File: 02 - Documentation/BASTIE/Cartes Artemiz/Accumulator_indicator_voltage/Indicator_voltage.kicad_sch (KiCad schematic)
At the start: 19 parts, among them J7 2P Droit 2-11-2022, Q1 NMOS SQ2348ES-T1_GE3

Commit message: Revert "Delete kicad_prl"
This reverts commit 9fe5be2906406c3c64afc6048a7ffd3d023d0e3c.
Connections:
- net 0: no longer PS1.4 (TRIM), PS1.6 (REMOTE_ON/OFF)
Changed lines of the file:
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@@
-	)
-	(junction
-		(at 88.9 43.18)
-		(diameter 0)
-		(color 0 0 0 0)
-	)
-	(junction
-		(at 142.24 43.18)
-		(diameter 0)
-		(color 0 0 0 0)
 	)
 	(junction
@@
 	(wire
 		(pts
-			(xy 88.9 43.18) (xy 88.9 48.26)
-		)
-		(stroke
-			(width 0)
-			(type default)
-		)
-	)
-	(wire
-		(pts
-			(xy 142.24 43.18) (xy 142.24 60.96)
+			(xy 142.24 40.64) (xy 142.24 60.96)
 		)
 		(stroke
@@
 	(wire
 		(pts
-			(xy 142.24 40.64) (xy 142.24 43.18)
-		)
-		(stroke
-			(width 0)
-			(type default)
-		)
-	)
-	(wire
-		(pts
 			(xy 142.24 38.1) (xy 142.24 33.02)
 		)
@@
 	(wire
 		(pts
-			(xy 138.43 43.18) (xy 142.24 43.18)
-		)
-		(stroke
-			(width 0)
-			(type default)
-		)
-	)
-	(wire
-		(pts
 			(xy 119.38 134.62) (xy 130.81 134.62)
 		)
@@
 	(wire
 		(pts
-			(xy 88.9 43.18) (xy 92.71 43.18)
-		)
-		(stroke
-			(width 0)
-			(type default)
-		)
-	)
-	(wire
-		(pts
 			(xy 59.69 146.05) (xy 64.77 146.05)
 		)
@@
 	(wire
 		(pts
-			(xy 88.9 40.64) (xy 88.9 43.18)
-		)
-		(stroke
+			(xy 88.9 40.64) (xy 88.9 48.26)
+		)
+		(stroke

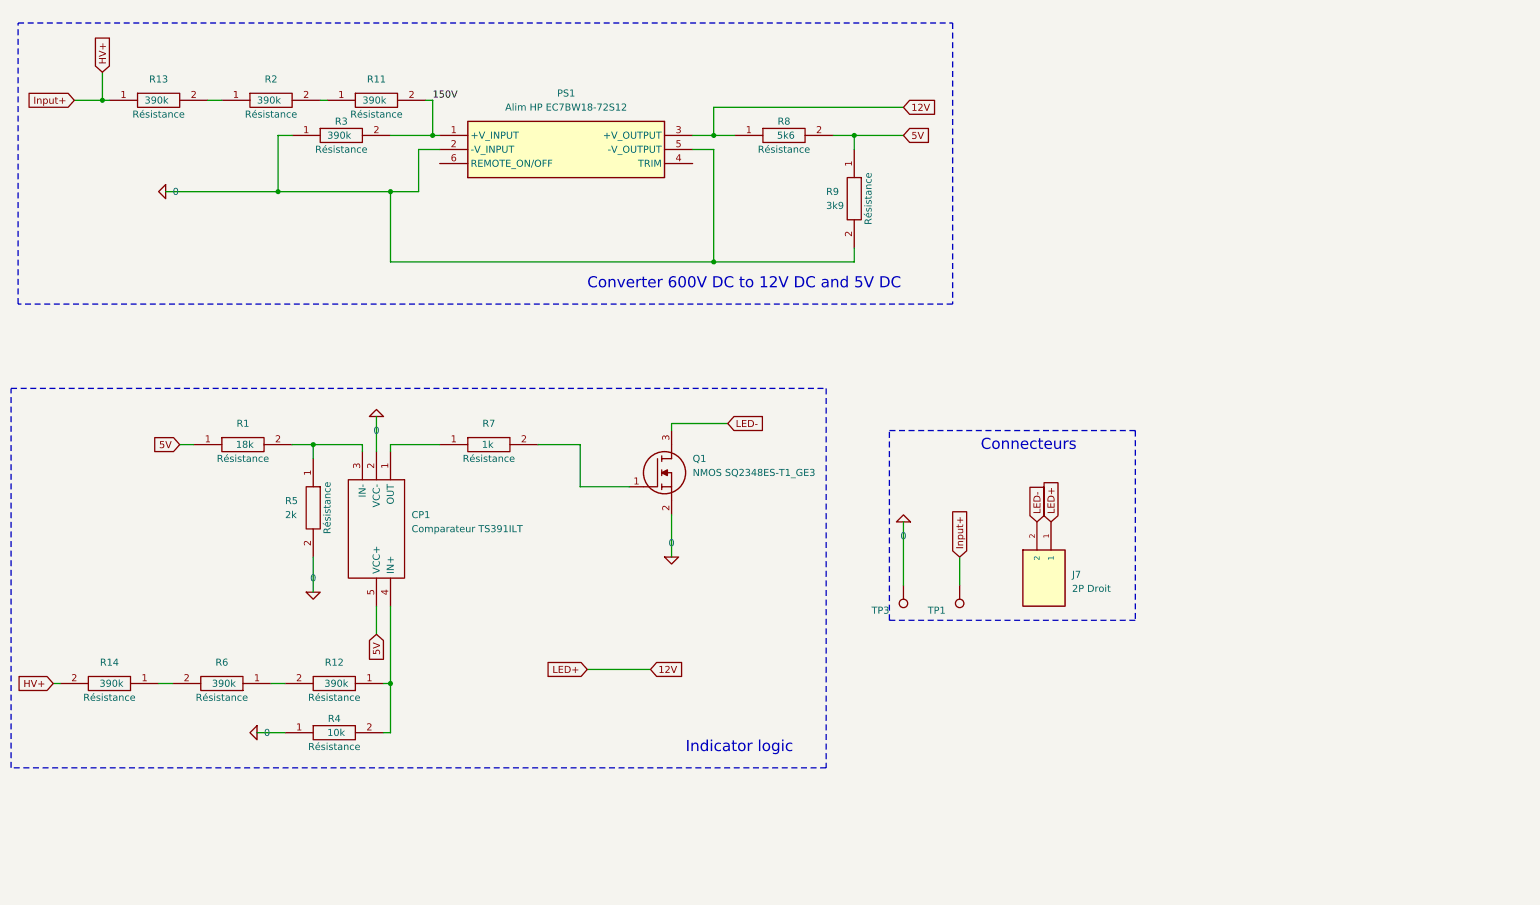
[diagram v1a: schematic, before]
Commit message: Working Voltage indicator
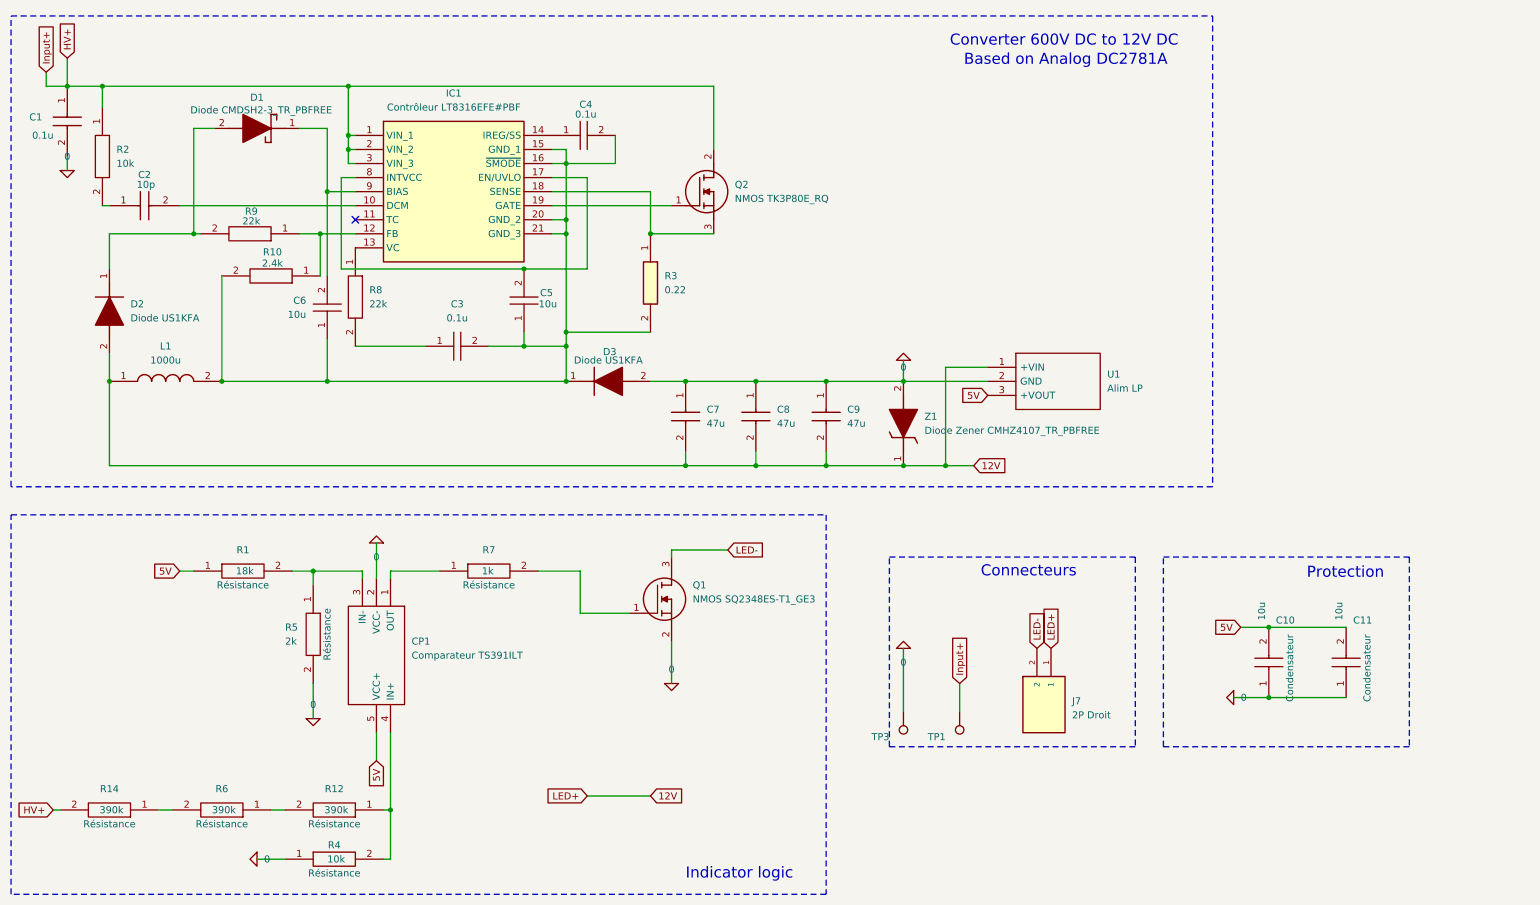
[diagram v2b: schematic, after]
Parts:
- removed PS1: Alim HP EC7BW18-72S12, EC7BW1872S12, symbol EPSAlib:Alim HP EC7BW18-72S12
- removed R11, R13, R2, R3: 390k, EPSA_lib:RESC3216X70N, symbol EPSA_lib:Résistance RK73H2BLTDD2152F
- removed R8: 5k6, EPSA_lib:RESC3216X70N, symbol EPSA_lib:Résistance RK73H2BLTDD2152F
- removed R9: 3k9, EPSA_lib:RESC3216X70N, symbol EPSA_lib:Résistance RK73H2BLTDD2152F
- added C1: 0.1u, CAPC4532X200N, symbol EPSAlib:Condensateur HV GCJ43DR72J104KXJ1L
- added C10, C11: 10u, EPSA:CAPC2012X130N, symbol EPSA_lib:Condensateur 0805Y1000104JXT
- added C2: 10p, CAPC3216X100N, symbol EPSAlib:Condensateur HV GRM31A5C2J100JW01D
- added C3, C4: 0.1u, EPSA_lib:CAPC2012X130N, symbol EPSAlib:Condensateur 0805Y1000104JXT
- added C5, C6: 10u, EPSA_lib:CAPC2012X130N, symbol EPSAlib:Condensateur 0805Y1000104JXT
- added C7, C8, C9: 47u, CAPC3225X270N, symbol EPSAlib:Condensateur GRM32ER61C476KE15K
- added D1: Diode CMDSH2-3_TR_PBFREE, SOD2512X110N, symbol EPSAlib:Diode CMDSH2-3_TR_PBFREE
- added D2, D3: Diode US1KFA, SODFL3618X143N, symbol EPSAlib:Diode US1KFA
- added IC1: Contrôleur LT8316EFE#PBF, LT8315EFEPBF, symbol EPSAlib:Contrôleur LT8316EFE#PBF
- added L1: 1000u, WE-PD_1260/1245/1280/121054, symbol EPSAlib:Bobine 7447709102
- added Q2: NMOS TK3P80E_RQ, TK3P80ERQ, symbol EPSAlib:NMOS TK3P80E_RQ
- added R10: 2.4k, EPSA_lib:RESC3216X70N, symbol EPSAlib:Résistance RK73H2BLTDD2152F
- added R2: 10k, EPSA_lib:RESC3216X70N, symbol EPSAlib:Résistance RK73H2BLTDD2152F
- added R3: 0.22, RESC1608X55N, symbol EPSAlib:Résistance RL0816S-R22-F
- added R8, R9: 22k, EPSA_lib:RESC3216X70N, symbol EPSAlib:Résistance RK73H2BLTDD2152F
- added U1: Alim LP TSR_0.5-2450, EPSA_lib:TSR-0.5-2433, symbol EPSAlib:Alim LP TSR_0.5-2450
- added Z1: Diode Zener CMHZ4107_TR_PBFREE, SOD3816X135N, symbol EPSAlib:Diode Zener CMHZ4107_TR_PBFREE
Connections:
- net 0: now also C1.2, C10.1, C11.1, C7.1, C8.1, C9.1, D3.2 (A), U1.2 (GND), Z1.2 (A)
- net 12V: now also C7.2, C8.2, C9.2, D2.2 (A), L1.1, U1.1 (+VIN), Z1.1 (K)
- net 5V: now also C10.2, C11.2, U1.3 (+VOUT)
- net HV+: now also C1.1, IC1.1 (VIN_1), IC1.2 (VIN_2), IC1.3 (VIN_3), Q2.2 (D), R2.1
- new net: C4.1, IC1.14 (IREG/SS)
- new net: C3.2, C4.2, C5.1, C6.1, D3.1 (K), IC1.15 (GND_1), IC1.16 (~{SMODE}), IC1.20 (GND_2), IC1.21 (GND_3), L1.2, R10.2, R3.2
- new net: C2.1, R2.2
- new net: C2.2, IC1.10 (DCM)
- new net: C6.2, D1.1 (K), IC1.9 (BIAS)
- new net: D1.2 (A), D2.1 (K), R9.2
- new net: IC1.13 (VC), R8.1
- new net: C3.1, R8.2
- new net: IC1.12 (FB), R10.1, R9.1
- new net: IC1.18 (SENSE), Q2.3 (S), R3.1
- new net: C5.2, IC1.17 (EN/UVLO), IC1.8 (INTVCC)
- new net: IC1.19 (GATE), Q2.1 (G)
- no-connect marks 0 -> 1
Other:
- note added: "Based on Analog DC2781A"
- note added: "Converter 600V DC to 12V DC"
- note added: "Protection"
- note removed: "Converter 600V DC to 12V DC and 5V DC"
- moved on the sheet: CP1, J7, Q1, R1, R12, R14, R4, R5, R6, R7, TP1, TP3

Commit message: TS et charger schematic pour école de ski français
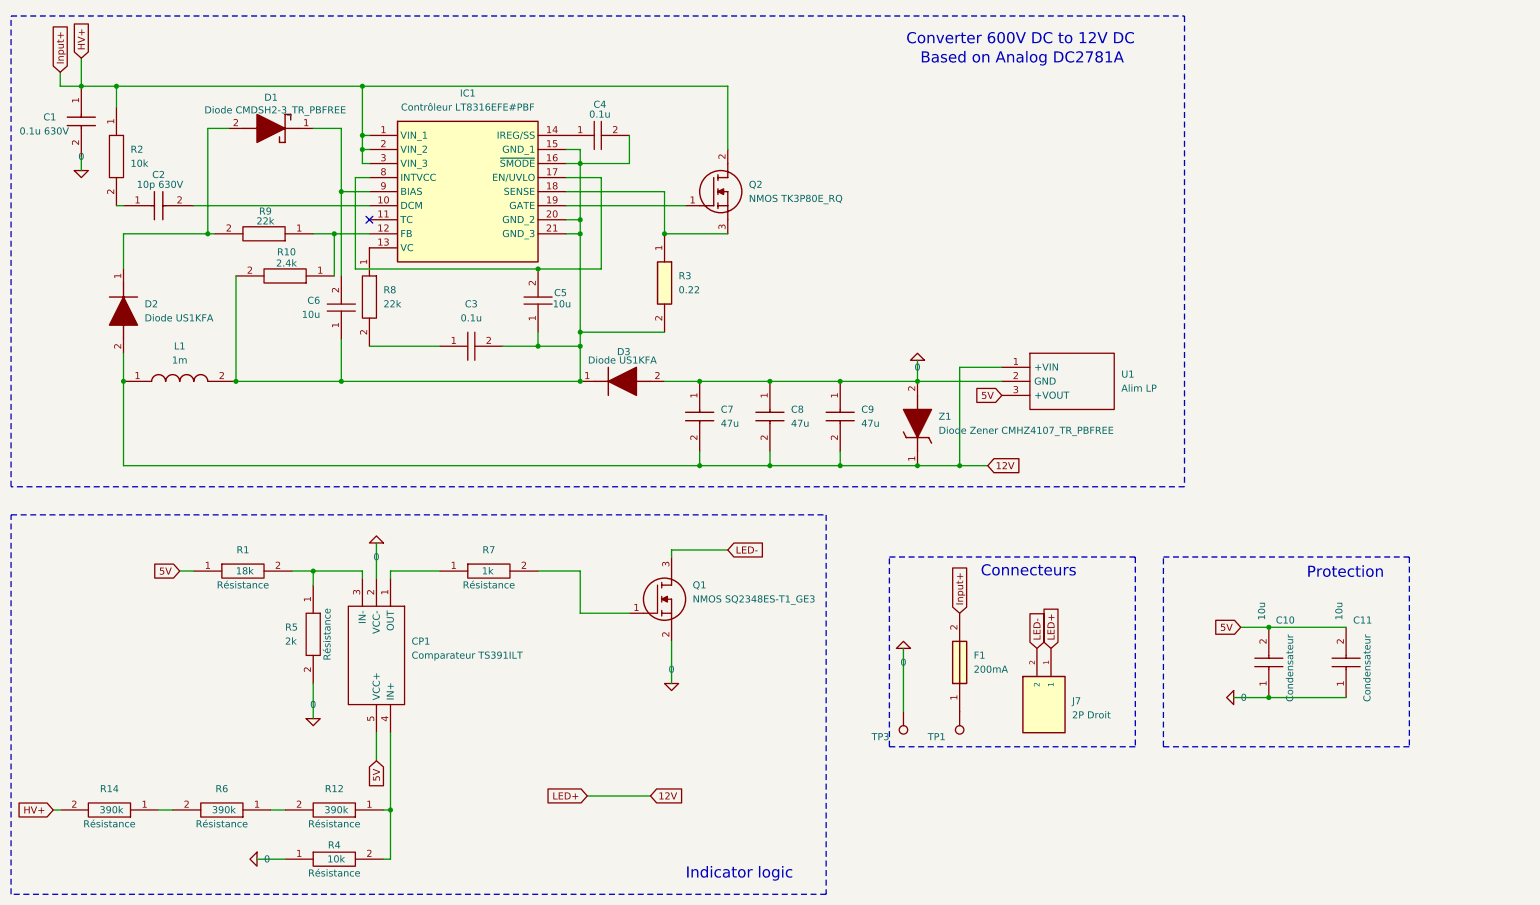
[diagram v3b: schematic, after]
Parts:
- added F1: 200mA, 0ADAP0200RE, symbol EPSAlib:Fusible 0ADAP0200-RE
- C1: value 0.1u -> 0.1u 630V
- C2: value 10p -> 10p 630V
- L1: value 1000u -> 1m
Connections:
- net HV+: now also F1.2; no longer TP1.1
- new net: F1.1, TP1.1
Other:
- moved on the sheet: C1, C2, C3, C4, C5, C6, C7, C8, C9, D1, D2, D3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

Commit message: Légères corrections Indicator Voltage
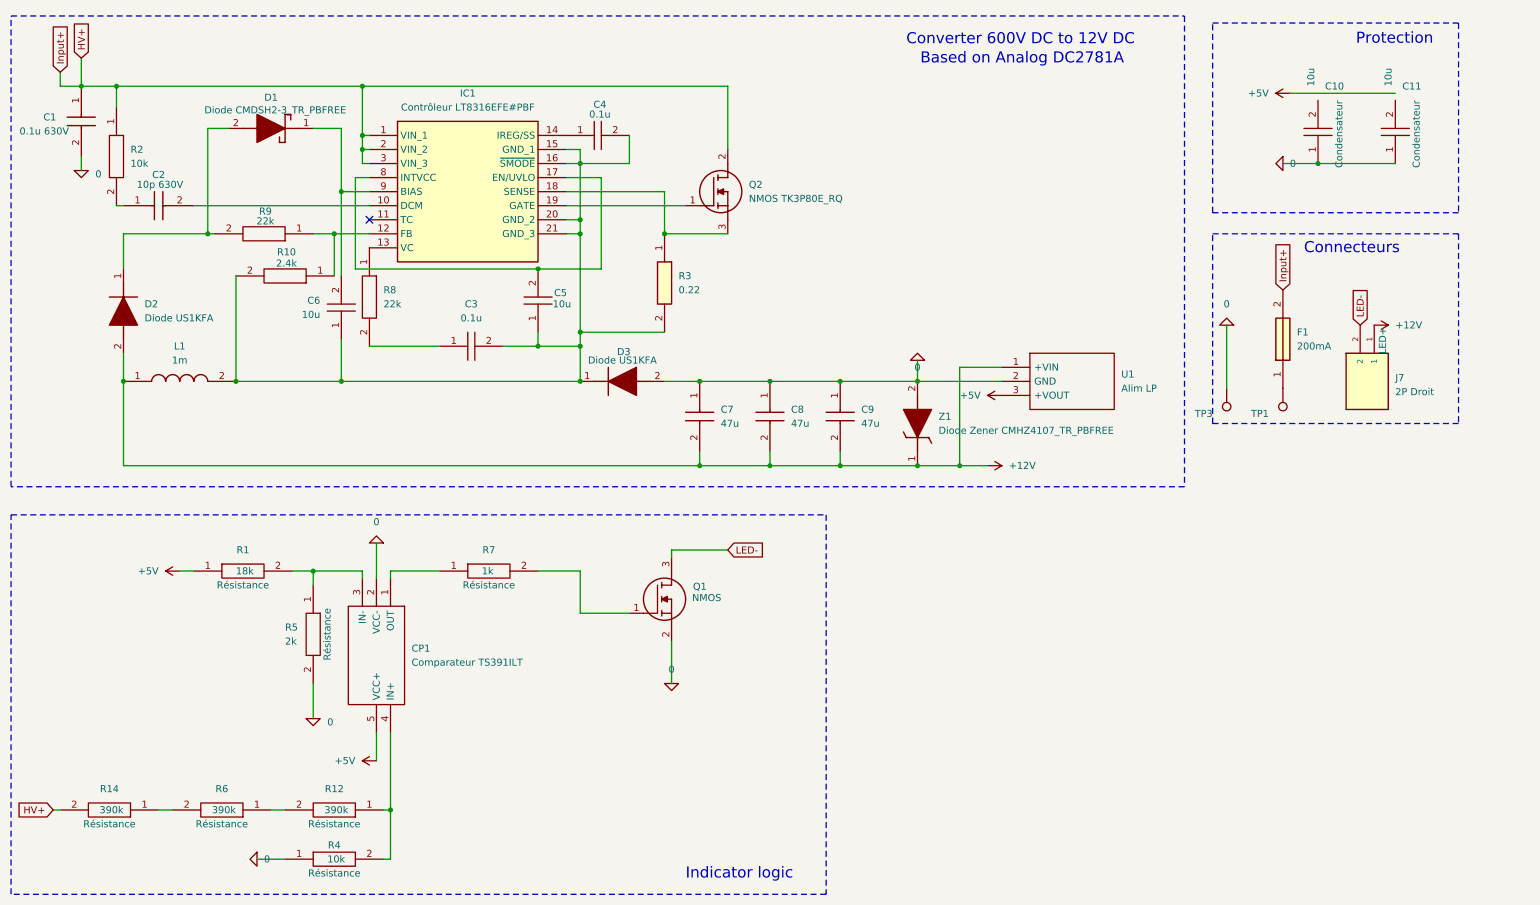
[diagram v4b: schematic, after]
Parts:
- C1: symbol EPSAlib:Condensateur HV GCJ43DR72J104KXJ1L -> EPSA_lib:Condensateur HV GCJ43DR72J104KXJ1L
- C2: symbol EPSAlib:Condensateur HV GRM31A5C2J100JW01D -> EPSA_lib:Condensateur HV GRM31A5C2J100JW01D
- C3, C4, C5, C6: symbol EPSAlib:Condensateur 0805Y1000104JXT -> EPSA_lib:Condensateur 0805Y1000104JXT
- C7, C8, C9: symbol EPSAlib:Condensateur GRM32ER61C476KE15K -> EPSA_lib:Condensateur GRM32ER61C476KE15K
- CP1: symbol EPSA_lib:Comparateur TS391ILT -> EPSA_lib:Dep_Comparateur TS391ILT; Render Name (none) -> Comparateur
- D1: symbol EPSAlib:Diode CMDSH2-3_TR_PBFREE -> EPSA_lib:Diode CMDSH2-3_TR_PBFREE
- D2, D3: symbol EPSAlib:Diode US1KFA -> EPSA_lib:Diode US1KFA
- F1: symbol EPSAlib:Fusible 0ADAP0200-RE -> EPSA_lib:Fusible 0ADAP0200-RE
- IC1: symbol EPSAlib:Contrôleur LT8316EFE#PBF -> EPSA_lib:Controleur LT8316EFE#PBF
- J7: Height (none) -> 10.66mm; Manufacturer_Name (none) -> Molex; Manufacturer_Part_Number (none) -> 22-11-2022; Mouser Part Number (none) -> 538-22-11-2022; Mouser Price/Stock (none) -> https://www.mouser.fr/ProductDetail/Molex/22-11-2022?qs=mrP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
- L1: symbol EPSAlib:Bobine 7447709102 -> EPSA_lib:Bobine 7447709102
- Q1: Render Name (none) -> NMOS
- Q2: symbol EPSAlib:NMOS TK3P80E_RQ -> EPSA_lib:NMOS TK3P80E_RQ
- R10, R2, R8, R9: symbol EPSAlib:Résistance RK73H2BLTDD2152F -> EPSA_lib:Résistance RK73H2BLTDD2152F
- R3: symbol EPSAlib:Résistance RL0816S-R22-F -> EPSA_lib:Résistance RL0816S-R22-F
- U1: symbol EPSAlib:Alim LP TSR_0.5-2450 -> EPSA_lib:Alim LP TSR_0.5-2450
- Z1: symbol EPSAlib:Diode Zener CMHZ4107_TR_PBFREE -> EPSA_lib:Diode Zener CMHZ4107_TR_PBFREE
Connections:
- net 12V renamed +12V
- net 5V renamed +5V
- net +5V: no longer C10.2, C11.2
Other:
- moved on the sheet: F1, J7, Q1, TP1, TP3

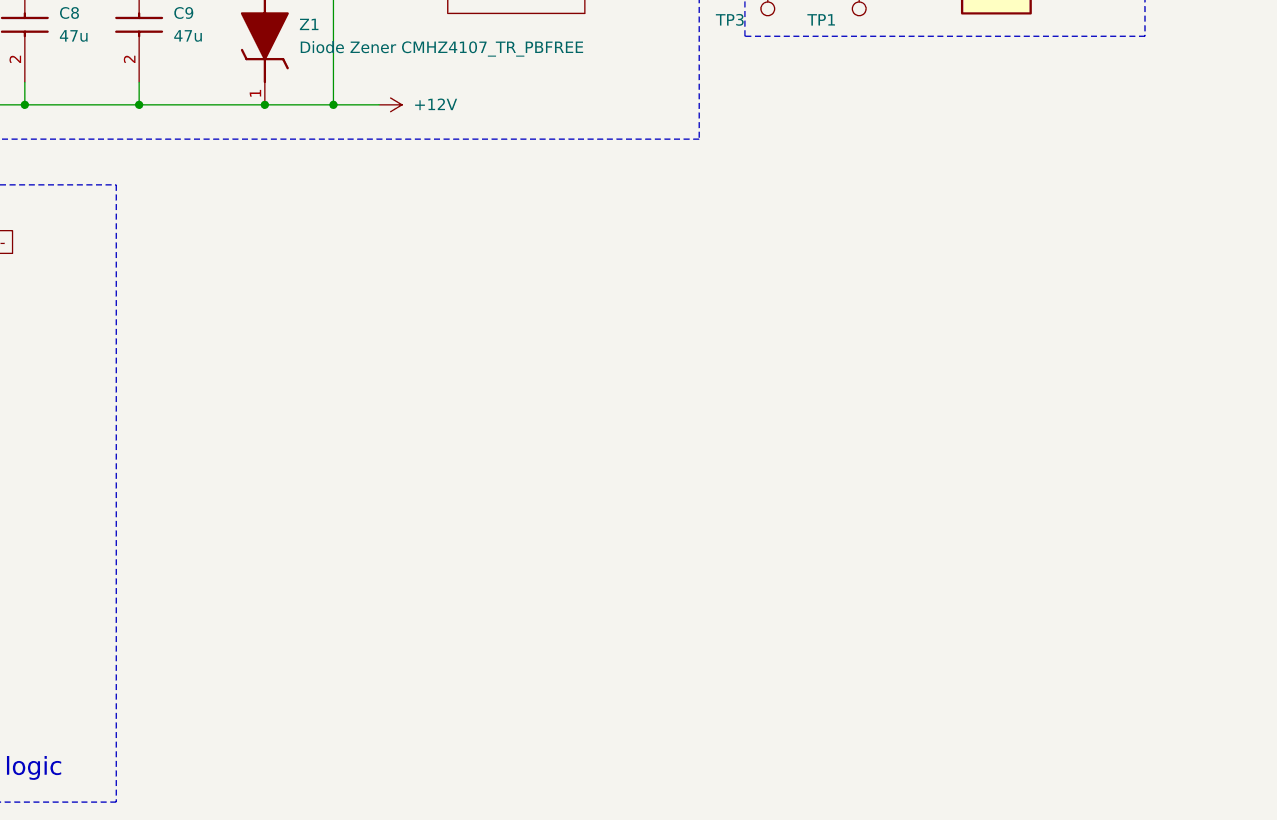
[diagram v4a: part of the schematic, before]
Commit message: Ajout sur la Voltage Indicator
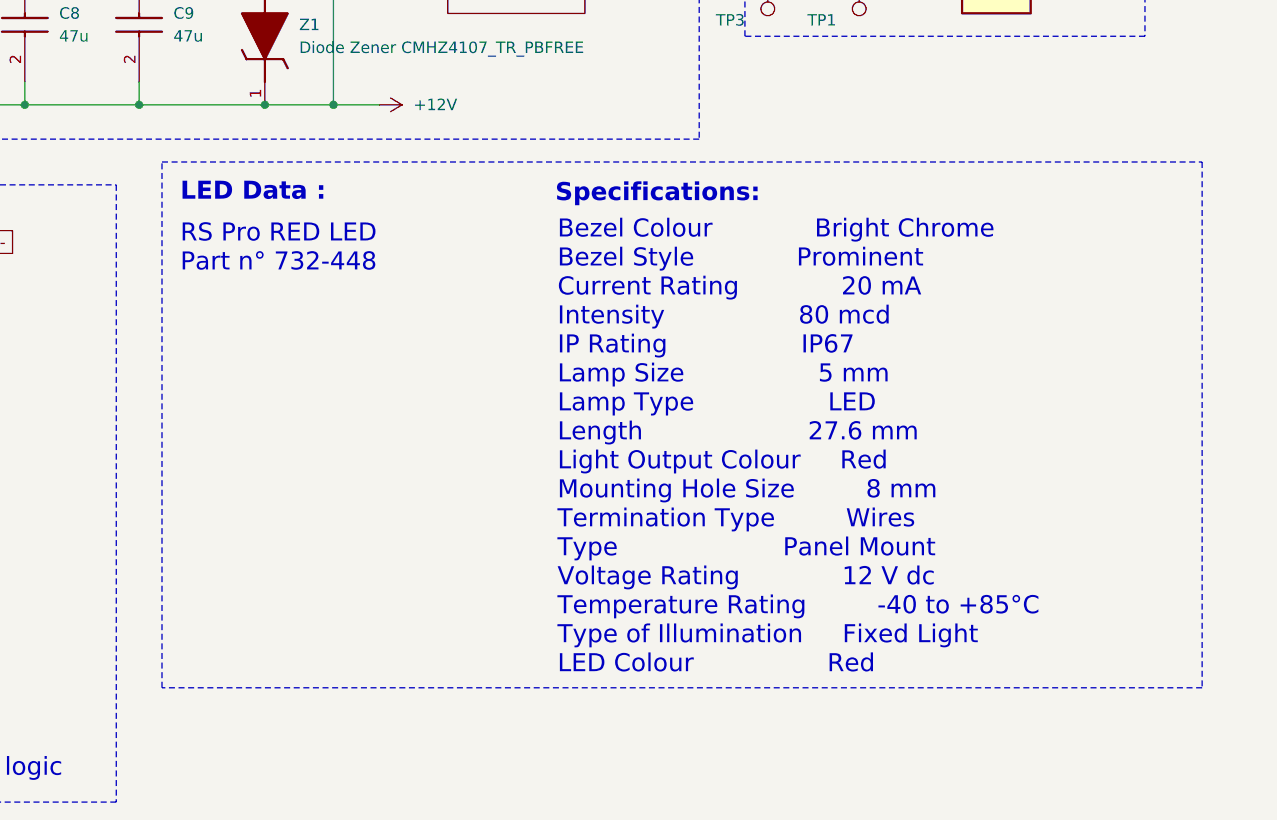
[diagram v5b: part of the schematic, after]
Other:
- note added: "Bezel Colour Bright Chrome Bezel Style Prominent Current Rating 20 mA Intensity 80 mcd IP Rating IP67 Lamp Size 5 mm Lamp Type LED Length 27.6 mm Light Output Colour Red Mounting Hole Size 8 mm Termination Type Wires Type Panel Mount Voltage Rating 12 V dc Temperature Rating -40 to +85°C Type of Illumination Fixed Light LED Colour Red"
- note added: "LED Data :"
- note added: "RS Pro RED LED Part n° 732-448"
- note added: "Specifications:"
